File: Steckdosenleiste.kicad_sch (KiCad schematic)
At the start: 0 parts

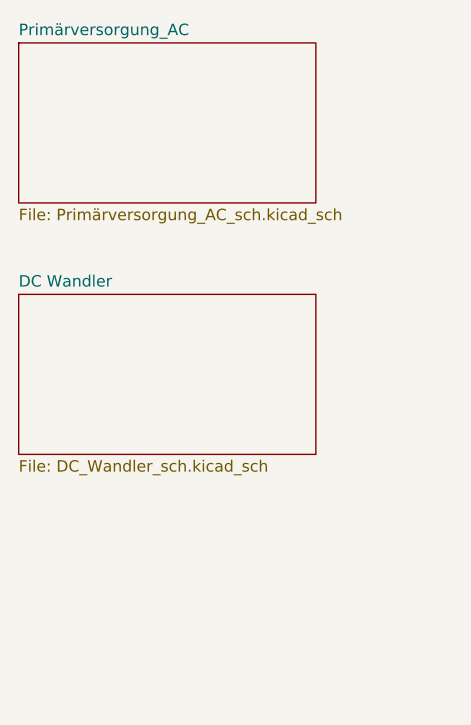
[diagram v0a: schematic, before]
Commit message: ESP32 Supply gestartet
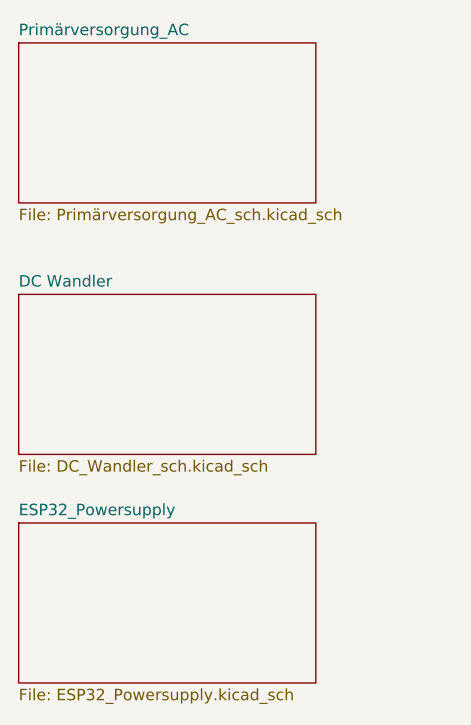
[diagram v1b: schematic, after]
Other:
- added sheet ESP32_Powersupply (ESP32_Powersupply.kicad_sch)
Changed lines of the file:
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@@
+		)
+	)
+	(sheet
+		(at 27.94 78.74)
+		(size 33.02 17.78)
+		(exclude_from_sim no)
+		(in_bom yes)
+		(on_board yes)
+		(dnp no)
+		(fields_autoplaced yes)
+		(stroke
+			(width 0.1524)
+			(type solid)
+		)
+		(fill
+			(color 0 0 0 0.0000)
+		)
+		(property "Sheetname" "ESP32_Powersupply"
+			(at 27.94 78.0284 0)
+			(effects
+				(font
+					(size 1.27 1.27)
+				)
+				(justify left bottom)
+			)
+		)
+		(property "Sheetfile" "ESP32_Powersupply.kicad_sch"
+			(at 27.94 97.1046 0)
+			(effects
+				(font
+					(size 1.27 1.27)
+				)
+				(justify left top)
+			)
+		)
+		(instances
+			(project "Steckdosenleiste"
+				(path "/54ba880c-6f45-4384-abe4-52c776779a10"
+					(page "4")
+				)
+			)
 		)
 	)
